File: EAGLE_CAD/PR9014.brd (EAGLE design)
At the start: 68.1 x 70.2 mm, 71 parts, among them J1 M3_SCREW_POST

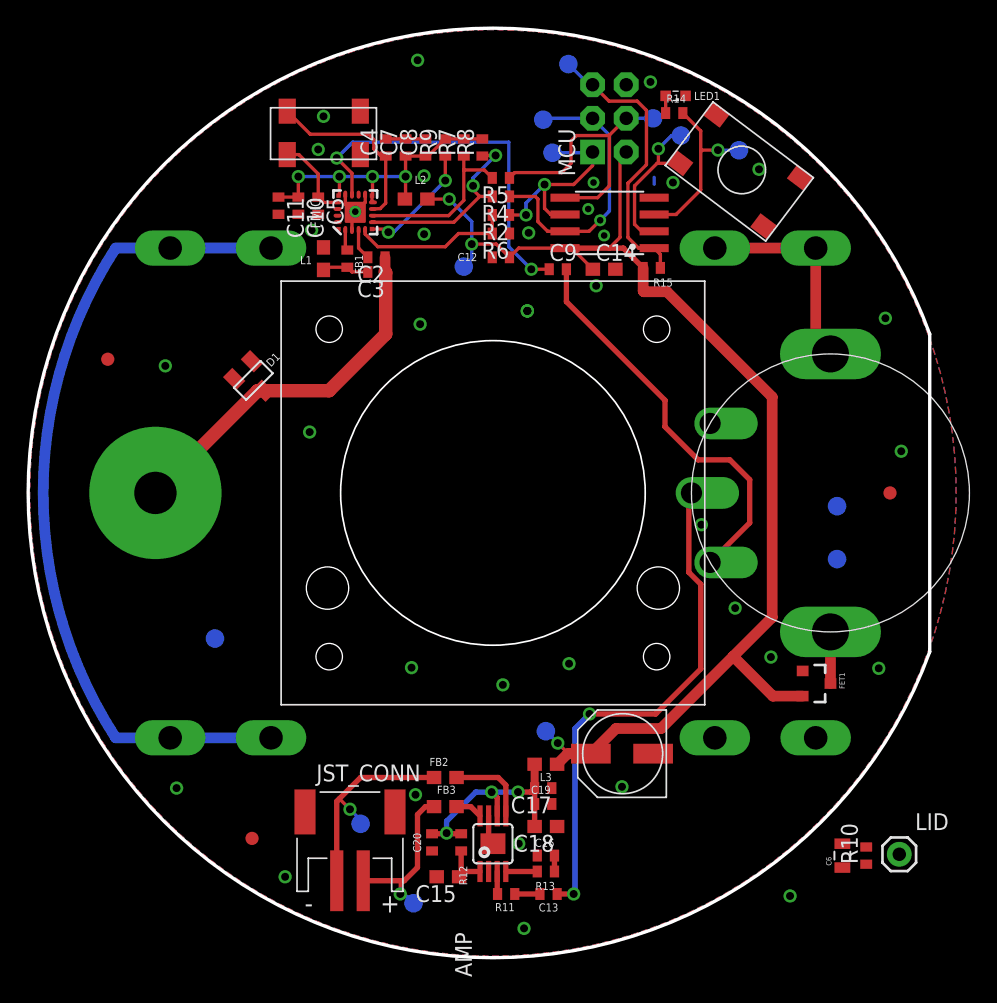
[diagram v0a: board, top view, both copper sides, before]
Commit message: Updated Library
Added AO3435, (Fet for reverse polarity) to the library and replaced it
in the sch and layout.
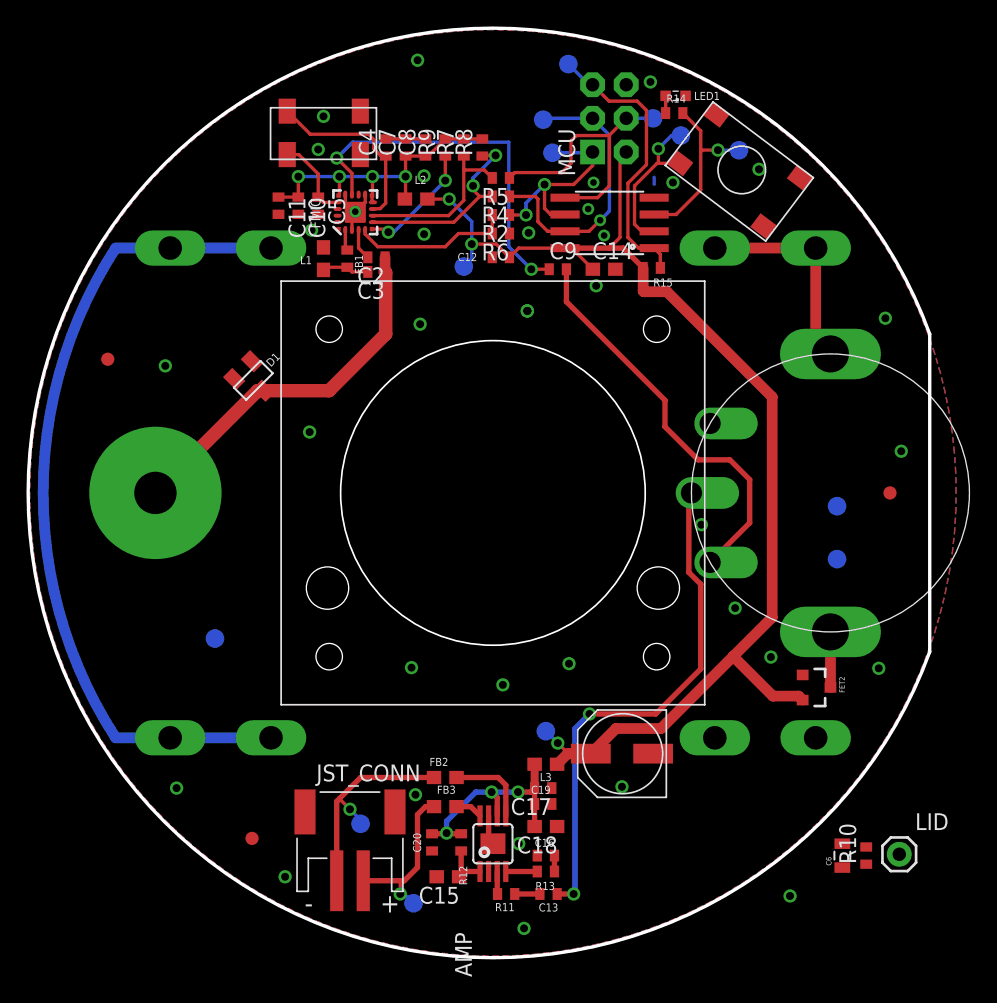
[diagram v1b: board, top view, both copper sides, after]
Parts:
- removed FET1: SI2333DDS, PubRadioLib:SI2333DDS
- added FET2: AO3435, PR_Parts_Library:AO3435
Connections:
- net GND: now also FET2.1; no longer FET1.1
- net N$34: now also FET2.3; no longer FET1.3
- net VCC: now also FET2.2; no longer FET1.2
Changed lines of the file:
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@@
 <element name="J1" library="PR_Parts_Library" package="M3_SCREW_POST" value="M3_SCREW_POST" x="9.5" y="35" locked="yes" smashed="yes"/>
 <element name="R1" library="PR_Parts_Library" package="RV170SF_TAIWANA_POT_SW" value="RV170SF_TAIWANA_POT_SW" x="60.5" y="35" locked="yes" rot="R270"/>
-<element name="FET1" library="PubRadioLib" package="SI2333DDS" value="SI2333DDS" x="59.4" y="20.6" rot="R270"/>
 <element name="MCU" library="SparkFun-DigitalIC" package="SO08-EIAJ" value="Tiny45-20-SMT" x="43.8" y="55.4" smashed="yes" rot="R90">
 <attribute name="PROD_ID" value="IC-09092" x="81.9" y="110.01" size="1.778" layer="27" rot="R90" display="off"/>
@@
 <element name="C17" library="resistor" package="C0402" value="1uf" x="38.8" y="12.7" rot="R180"/>
 <element name="C9" library="resistor" package="C0402" value="1uF" x="39.9" y="51.9"/>
+<element name="FET2" library="PR_Parts_Library" package="AO3435" value="AO3435" x="59.4" y="20.3" rot="R270"/>
 </elements>
 <signals>
@@
 <contactref element="C16" pad="1"/>
 <contactref element="C6" pad="2"/>
-<contactref element="FET1" pad="1"/>
 <contactref element="MCU" pad="4"/>
 <contactref element="ISP" pad="6"/>
@@
 <wire x1="23.85" y1="56.8" x2="24.6" y2="56.25" width="0.254" layer="1"/>
 <via x="21.3" y="54.85" extent="1-16" drill="0.6"/>
+<contactref element="FET2" pad="1"/>
 <wire x1="57.45" y1="4.55" x2="61.4" y2="8.5" width="0" layer="19" extent="1-1"/>
 <wire x1="59.384" y1="16.5" x2="61.4" y2="8.5" width="0" layer="19" extent="1-1"/>
@@
 <signal name="VCC">
 <contactref element="L3" pad="1"/>
-<contactref element="FET1" pad="2"/>
 <contactref element="MCU" pad="8"/>
 <contactref element="L2" pad="1"/>
@@
 <wire x1="46.4" y1="50.2" x2="46.35" y2="50.25" width="0.8128" layer="1"/>
 <wire x1="46.35" y1="50.25" x2="46.35" y2="52" width="0.8128" layer="1"/>
-<wire x1="58.4" y1="19.65" x2="56.15" y2="19.65" width="0.8128" layer="1"/>
 <wire x1="56.15" y1="19.65" x2="53.15" y2="22.65" width="0.8128" layer="1"/>
 <via x="31.7" y="57.2" extent="1-16" drill="0.6"/>
@@
 <wire x1="32.8" y1="52.1" x2="33.4" y2="52.7" width="0.254" layer="16"/>
 <wire x1="33.4" y1="52.7" x2="33.4" y2="53.8" width="0.254" layer="16"/>
+<contactref element="FET2" pad="2"/>
+<wire x1="56.15" y1="19.65" x2="58.1" y2="19.65" width="0.8128" layer="1"/>
+<wire x1="58.1" y1="19.65" x2="58.4" y2="19.35" width="0.8128" layer="1"/>
 </signal>
 <signal name="N$4">
@@
 <signal name="N$34">
 <contactref element="R1" pad="SW_IN"/>
-<contactref element="FET1" pad="3"/>
-<wire x1="60.5" y1="24.5" x2="60.5" y2="20.6" width="0.8128" layer="1"/>
+<contactref element="FET2" pad="3"/>
+<wire x1="60.5" y1="20.3" x2="60.5" y2="24.5" width="0.8128" layer="1"/>
 </signal>
 <signal name="N$35">

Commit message: Updated Layout
Small things
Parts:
- moved C20 0.50 mm to (29.9, 8.60)
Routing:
- net GND: track 12.9 -> 11.3 mm, vias 36 -> 39
- net N$18: track 17.5 -> 18.1 mm
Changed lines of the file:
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@@
 <?xml version="1.0" encoding="utf-8"?>
 <!DOCTYPE eagle SYSTEM "eagle.dtd">
-<eagle version="7.2.0">
+<eagle version="6.6.0">
 <drawing>
 <settings>
@@
 <pass name="Default">
 <param name="RoutingGrid" value="50mil"/>
-<param name="AutoGrid" value="1"/>
-<param name="Efforts" value="0"/>
-<param name="TopRouterVariant" value="1"/>
 <param name="tpViaShape" value="round"/>
 <param name="PrefDir.1" value="|"/>
@@
 <attribute name="VALUE" x="39.816" y="12.897" size="0.4064" layer="27" rot="R180"/>
 </element>
-<element name="C20" library="resistor" package="C0402" value="100pf" x="30.4" y="8.6" smashed="yes" rot="R90">
-<attribute name="NAME" x="29.5745" y="7.838" size="0.6096" layer="25" rot="R90"/>
-<attribute name="VALUE" x="31.797" y="7.584" size="0.4064" layer="27" rot="R90"/>
+<element name="C20" library="resistor" package="C0402" value="100pf" x="29.9" y="8.6" smashed="yes" rot="R90">
+<attribute name="NAME" x="29.0745" y="7.838" size="0.6096" layer="25" rot="R90"/>
+<attribute name="VALUE" x="31.297" y="7.584" size="0.4064" layer="27" rot="R90"/>
 </element>
 <element name="LID" library="SparkFun-Connectors" package="1X01" value="M01PTH" x="65.7" y="7.7"/>
@@
 <contactref element="C11" pad="2"/>
 <via x="55.1" y="59.45" extent="1-16" drill="0.6"/>
-<via x="24.6" y="56.25" extent="1-16" drill="0.5"/>
 <via x="37.6" y="48.75" extent="1-16" drill="0.6"/>
 <via x="29.5" y="47.75" extent="1-16" drill="0.6"/>
@@
 <wire x1="24.85" y1="54.865" x2="24.85" y2="53.5" width="0.254" layer="1"/>
 <wire x1="24.85" y1="53.5" x2="25.55" y2="52.8" width="0.254" layer="1"/>
-<wire x1="24.35" y1="54.865" x2="24.35" y2="56" width="0.254" layer="1"/>
-<wire x1="24.35" y1="56" x2="24.6" y2="56.25" width="0.254" layer="1"/>
 <wire x1="25.35" y1="57.535" x2="25.35" y2="56.95" width="0.254" layer="1"/>
-<wire x1="25.35" y1="56.95" x2="24.6" y2="56.2" width="0.254" layer="1"/>
-<wire x1="23.85" y1="57.535" x2="23.85" y2="56.8" width="0.254" layer="1"/>
-<wire x1="23.85" y1="56.8" x2="24.6" y2="56.25" width="0.254" layer="1"/>
 <via x="21.3" y="54.85" extent="1-16" drill="0.6"/>
 <contactref element="FET2" pad="1"/>
+<via x="24.2" y="55.85" extent="1-16" drill="0.1"/>
+<wire x1="23.85" y1="57.535" x2="23.85" y2="56.95" width="0.2" layer="1"/>
+<via x="25" y="56.65" extent="1-16" drill="0.1"/>
+<wire x1="24.35" y1="54.865" x2="24.35" y2="55.7" width="0.2" layer="1"/>
+<wire x1="24.35" y1="55.7" x2="24.2" y2="55.85" width="0.2" layer="1"/>
+<wire x1="25.35" y1="56.95" x2="25.3" y2="56.95" width="0.2" layer="1"/>
+<wire x1="25.3" y1="56.95" x2="25" y2="56.65" width="0.2" layer="1"/>
+<via x="25" y="55.85" extent="1-16" drill="0.1"/>
+<via x="24.2" y="56.65" extent="1-16" drill="0.1"/>
+<wire x1="23.85" y1="56.95" x2="23.9" y2="56.95" width="0.2" layer="1"/>
+<wire x1="23.9" y1="56.95" x2="24.2" y2="56.65" width="0.2" layer="1"/>
 <wire x1="57.45" y1="4.55" x2="61.4" y2="8.5" width="0" layer="19" extent="1-1"/>
 <wire x1="59.384" y1="16.5" x2="61.4" y2="8.5" width="0" layer="19" extent="1-1"/>
@@
 <contactref element="C18" pad="2"/>
 <contactref element="C17" pad="2"/>
-<wire x1="30.4" y1="9.25" x2="31.45" y2="9.25" width="0.4064" layer="1"/>
-<wire x1="31.45" y1="9.25" x2="31.5" y2="9.3" width="0.4064" layer="1"/>
-<via x="31.5" y="9.3" extent="1-16" drill="0.6"/>
-<wire x1="31.5" y1="9.3" x2="31.5" y2="10.2" width="0.4064" layer="16"/>
-<wire x1="32.6" y1="9.25" x2="31.55" y2="9.25" width="0.4064" layer="1"/>
-<wire x1="31.55" y1="9.25" x2="31.5" y2="9.3" width="0.4064" layer="1"/>
 <wire x1="35.325" y1="10.6" x2="35.325" y2="11.975" width="0.4064" layer="1"/>
 <wire x1="35.325" y1="11.975" x2="34.9" y2="12.4" width="0.4064" layer="1"/>
 <via x="34.9" y="12.4" extent="1-16" drill="0.6"/>
 <wire x1="34.9" y1="12.4" x2="33.7" y2="12.4" width="0.4064" layer="16"/>
-<wire x1="33.7" y1="12.4" x2="31.5" y2="10.2" width="0.4064" layer="16"/>
+<wire x1="33.7" y1="12.4" x2="31.3" y2="10" width="0.4064" layer="16"/>
 <wire x1="38.15" y1="12.7" x2="37.85" y2="12.4" width="0.4064" layer="1"/>
 <wire x1="37.85" y1="12.4" x2="36.9" y2="12.4" width="0.4064" layer="1"/>
@@
 <wire x1="38.15" y1="9.8" x2="38.15" y2="11.5" width="0.4064" layer="1"/>
 <wire x1="38.15" y1="11.5" x2="38.15" y2="12.7" width="0.4064" layer="1"/>
+<wire x1="31.3" y1="10" x2="31.3" y2="9.3" width="0.4064" layer="16"/>
+<via x="31.3" y="9.3" extent="1-16" drill="0.6" diameter="0.4064"/>
+<wire x1="31.3" y1="9.3" x2="32.55" y2="9.3" width="0.4064" layer="1"/>
+<wire x1="32.55" y1="9.3" x2="32.6" y2="9.25" width="0.4064" layer="1"/>
+<wire x1="31.3" y1="9.3" x2="29.95" y2="9.3" width="0.4064" layer="1"/>
+<wire x1="29.95" y1="9.3" x2="29.9" y2="9.25" width="0.4064" layer="1"/>
 </signal>
 <signal name="N$20">
@@
 <contactref element="C15" pad="1"/>
 <wire x1="34.025" y1="6.4" x2="32.85" y2="6.4" width="0.4064" layer="1"/>
-<wire x1="32.85" y1="6.4" x2="32.45" y2="6" width="0.4064" layer="1"/>
+<wire x1="32.85" y1="6.4" x2="32.6" y2="6.15" width="0.4064" layer="1"/>
 <wire x1="32.6" y1="7.95" x2="32.6" y2="6.15" width="0.4064" layer="1"/>
 <wire x1="32.6" y1="6.15" x2="32.45" y2="6" width="0.4064" layer="1"/>
@@
 <contactref element="C3" pad="1"/>
 <wire x1="26.85" y1="52.8" x2="26.85" y2="51.7" width="0.8128" layer="1"/>
-<wire x1="9.5" y1="35" x2="17.22218125" y2="42.72218125" width="1.016" layer="1"/>
-<wire x1="17.22218125" y1="42.72218125" x2="17.677815625" y2="42.72218125" width="1.016" layer="1"/>
 <wire x1="17.677815625" y1="42.72218125" x2="22.62218125" y2="42.72218125" width="1.016" layer="1"/>
 <wire x1="22.62218125" y1="42.72218125" x2="26.9" y2="47" width="1.016" layer="1"/>
 <wire x1="26.9" y1="47" x2="26.9" y2="51.65" width="1.016" layer="1"/>
 <wire x1="26.9" y1="51.65" x2="26.85" y2="51.7" width="1.016" layer="1"/>
+<wire x1="9.5" y1="35" x2="9.955634375" y2="35" width="0.8128" layer="1"/>
+<wire x1="9.955634375" y1="35" x2="17.677815625" y2="42.72218125" width="0.8128" layer="1"/>
 </signal>
 <signal name="N$16" class="1">
@@
 <contactref element="FB3" pad="1"/>
 <contactref element="TP7" pad="TP"/>
-<wire x1="30.55" y1="11.3" x2="29.9" y2="11.3" width="0.4064" layer="1"/>
-<wire x1="29.9" y1="11.3" x2="29.3" y2="10.7" width="0.4064" layer="1"/>
-<wire x1="29.3" y1="10.7" x2="29.3" y2="6.7" width="0.4064" layer="1"/>
-<wire x1="29.3" y1="6.7" x2="28.3" y2="5.7" width="0.4064" layer="1"/>
+<wire x1="30.55" y1="11.3" x2="29.4" y2="11.3" width="0.4064" layer="1"/>
 <wire x1="28.3" y1="5.7" x2="28" y2="5.7" width="0.4064" layer="1"/>
 <wire x1="28" y1="5.7" x2="25.2" y2="5.7" width="0.4064" layer="1"/>
@@
 <via x="28" y="4.7" extent="1-16" drill="0.6"/>
 <wire x1="28" y1="4.7" x2="28" y2="5.7" width="0.254" layer="1"/>
+<wire x1="29.4" y1="11.3" x2="29" y2="10.9" width="0.4064" layer="1"/>
+<wire x1="29" y1="10.9" x2="29" y2="6.4" width="0.4064" layer="1"/>
+<wire x1="29" y1="6.4" x2="28.3" y2="5.7" width="0.4064" layer="1"/>
 </signal>
 <signal name="N$9">

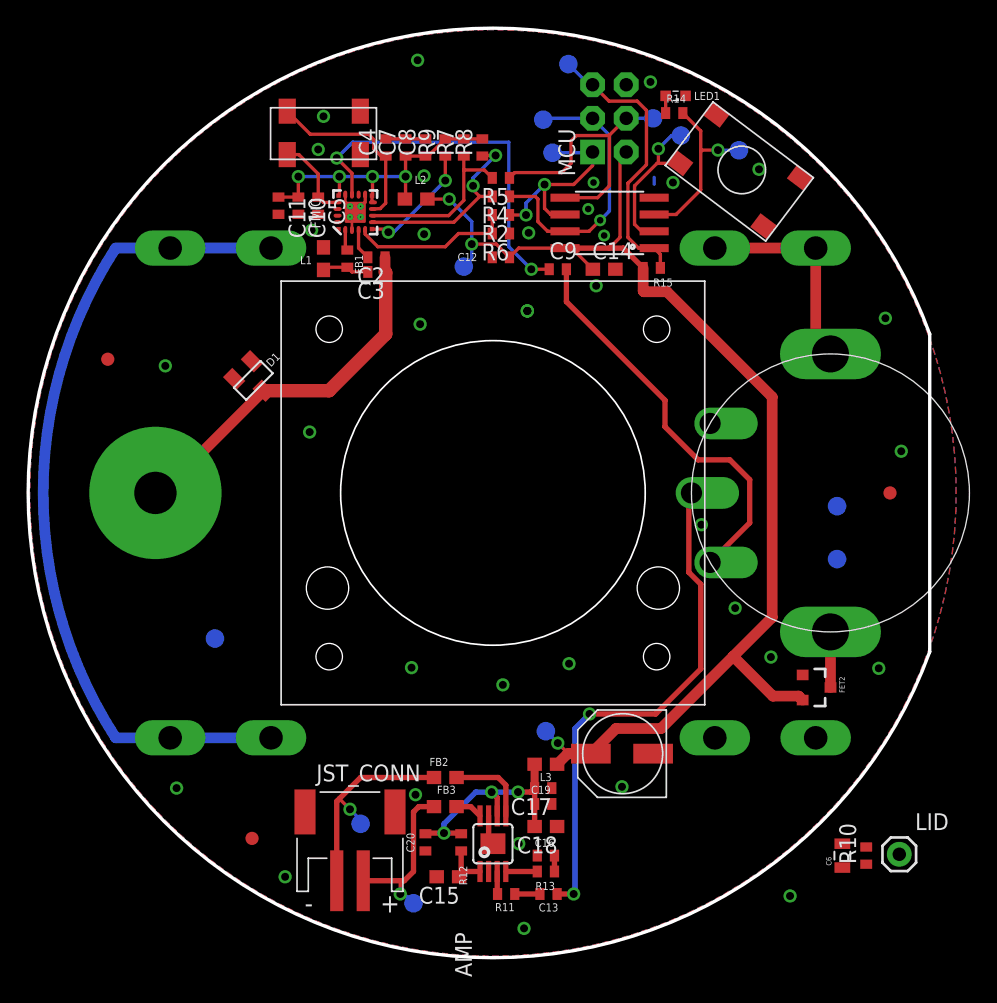
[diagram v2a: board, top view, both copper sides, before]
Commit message: bunch of changes
couple library updates, the most notable of which is the button
footprint

then

a bunch of layout edits
mostly in response to andy’s feedback
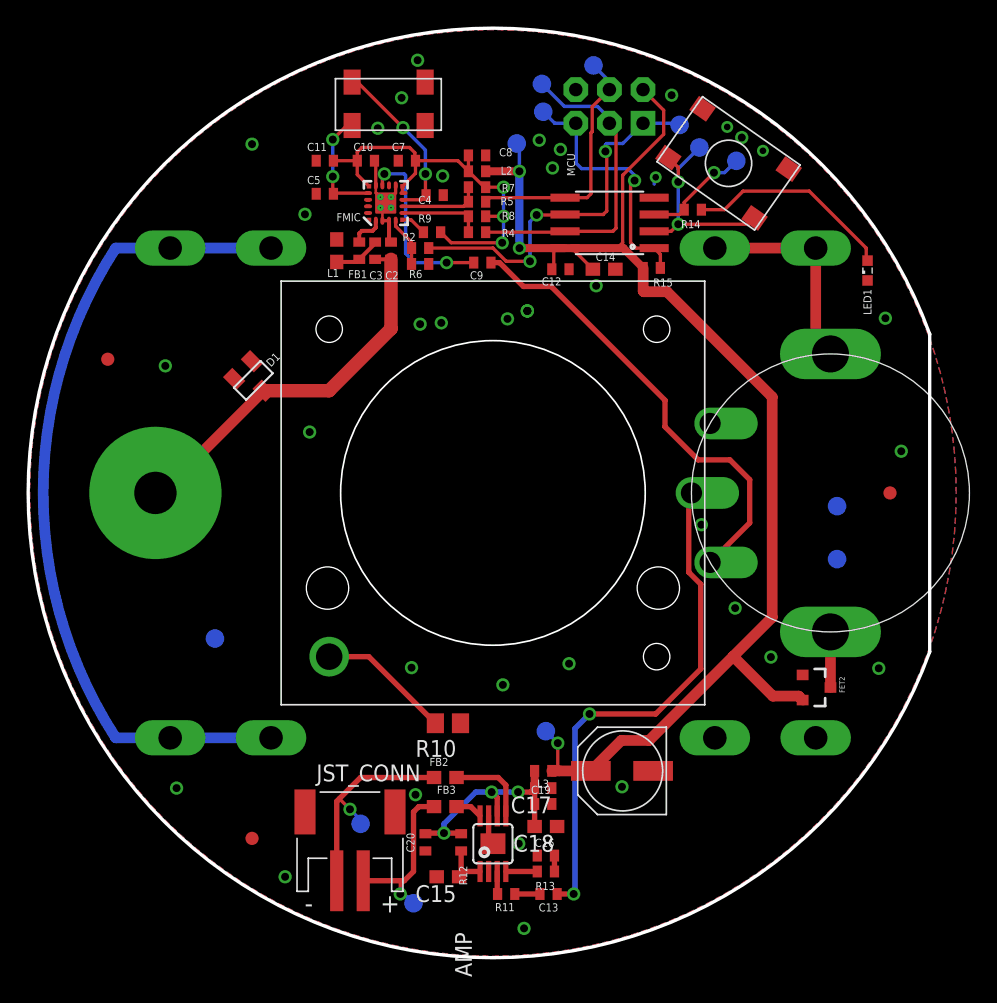
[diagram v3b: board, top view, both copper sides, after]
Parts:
- removed C6: (no value), SparkFun-Passives:0805
- removed LID: M01PTH, SparkFun-Connectors:1X01
- removed SPEAKER: CE32A_FOR_JST, PR_Parts_Library:CE32A_FOR_JST
- added SW1: C&K_PTS645, PR_Parts_Library:C&K_TACTILE_SWITCH
- L2: value 2.5k@100MHz -> 2.2k@100MHz; device SparkFun-Passives:0603 -> SparkFun-Passives:C0402
- L3: value 2.5 kOhm @ 100MHz -> 2.2 kOhm @ 100MHz; device SparkFun-Passives:0603 -> SparkFun-Passives:C0402
- R10: device resistor:R0402 -> resistor:R0805
- U$1: value C&KPTS6465 -> (none); device PR_Parts_Library:C&K_TACTILE_SWITCH -> PR_Parts_Library:CE32A_FOR_JST
- moved R10 33.1 mm to (31.6, 17.6), turned to 180 degrees
- moved U$1 30.8 mm to (35.0, 35.0), turned to 0 degrees
- moved LED1 19.6 mm to (63.3, 51.8), turned to 90 degrees
- moved TP5 10.1 mm to (36.8, 61.4)
- moved TP10 9.83 mm to (49.1, 62.8)
- moved R14 7.43 mm to (50.1, 56.4), turned to 180 degrees
- moved R2 6.59 mm to (29.5, 53.5)
- moved R6 6.52 mm to (29.5, 52.3)
- moved R9 6.48 mm to (30.4, 54.7), turned to 0 degrees
- moved C10 6.13 mm to (25.4, 60.1), turned to 0 degrees
- moved TP13 6.02 mm to (42.6, 67.3)
- moved C9 5.72 mm to (34.2, 52.4)
- moved U$6 5.37 mm to (27.2, 64.5)
- moved R8 5.22 mm to (33.8, 55.9), turned to 0 degrees
- moved C4 5.16 mm to (30.6, 57.5), turned to 0 degrees
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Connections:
- removed net N$35: C6.1, R10.1
- net GND: now also R10.1, SW1.P$1, SW1.P$2; no longer C6.2, U$1.P$1
- net N$8: now also U$1.LID_GND; no longer LID.1
- net SW: now also SW1.P$3, SW1.P$4; no longer U$1.P$3
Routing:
- net N$7: track 1.30 -> 15.8 mm
- net N$9: track 28.4 -> 13.9 mm
- net !RST: track 16.0 -> 29.1 mm, vias 2 -> 3
- net VCC: track 94.1 -> 104.9 mm
- net N$8: track 0.00 -> 10.1 mm
- net SCLK-L: track 14.9 -> 6.22 mm, vias 2 -> 0
- net !RST-L: track 12.1 -> 3.76 mm
- net 3.3V: track 24.2 -> 32.2 mm, vias 4 -> 3
- net !SEN-L: track 9.10 -> 1.97 mm, vias 2 -> 0
- net SDIO-L: track 13.1 -> 6.16 mm
- net LED/PB4: track 13.6 -> 8.21 mm
- net SW: track 12.1 -> 16.6 mm, vias 1 -> 2
- net A_IN: track 30.5 -> 35.0 mm
- net SCLK: track 21.6 -> 24.7 mm, vias 1 -> 0
- net N$2: track 6.33 -> 8.66 mm, vias 0 -> 2
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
